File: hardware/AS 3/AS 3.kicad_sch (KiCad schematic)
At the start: 84 parts, among them J1 Conn_02x03_Odd_Even, J2 Conn_01x04, J3 USB_C_Receptacle_USB2.0_16P, Q1 PSMN5R2-60YL, SW1 SW_Push, SW2 SW_Push, U1 ESP32-S3-WROOM-1, U2 LM74610QDGKTQ1, U3 LMR604205SRAKRQ1, U4 TPS62901RPJR, U5 BME280, U6 TPS2121RUXR

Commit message: Update schematic
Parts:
- removed U5: BME280, BME280:PSON65P250X250X100-8N, symbol BME280:BME280
- added U5: BME280, Package_LGA:Bosch_LGA-8_2.5x2.5mm_P0.65mm_ClockwisePinNumbering, symbol Sensor:BME280
- C23: symbol PCM_JLCPCB-Capacitors:0603,100nF -> Device:C_Small
- C24: value 10uF -> 10u; symbol PCM_JLCPCB-Capacitors:1206,10uF -> Device:C_Small; Type X7R Ceramic -> (none)
- D1, D4, D5, D6, D7: value Green -> LED_Small
- R17, R6: value 4.7K -> 1k
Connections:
- net +3.3V: now also U5.2 (CSB), U5.6 (VDDIO), U5.8 (VDD)
- net GND: now also U3.7 (MODE_SYNC), U5.1 (GND), U5.5 (SDO), U5.7 (GND)
- net SCL: now also U5.4 (SCK)
- net SDA: now also U5.3 (SDI)
- net at R14.1, U3.8 (RT): no longer U3.7 (MODE_SYNC)
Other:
- moved on the sheet: C11, C12, C23, C24, R15, R16

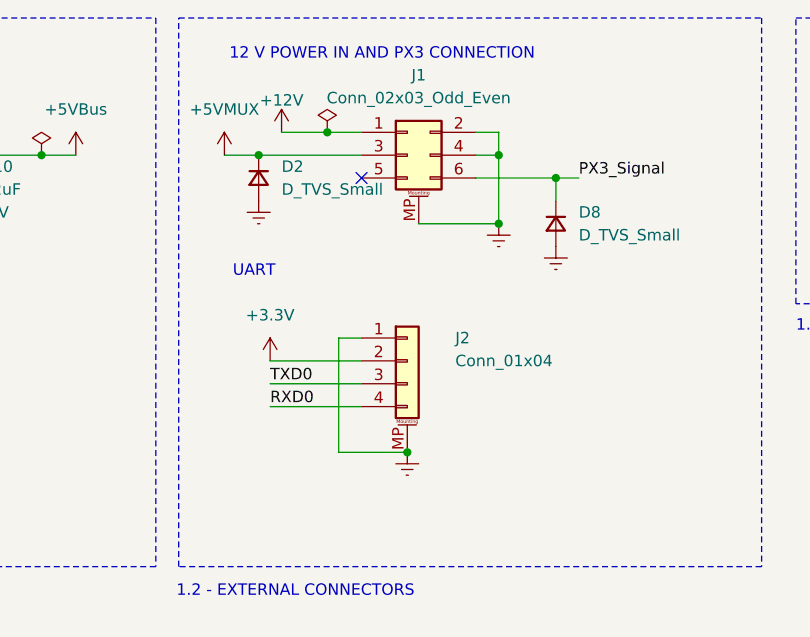
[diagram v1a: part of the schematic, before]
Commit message: time to make vias bigger and order this thing
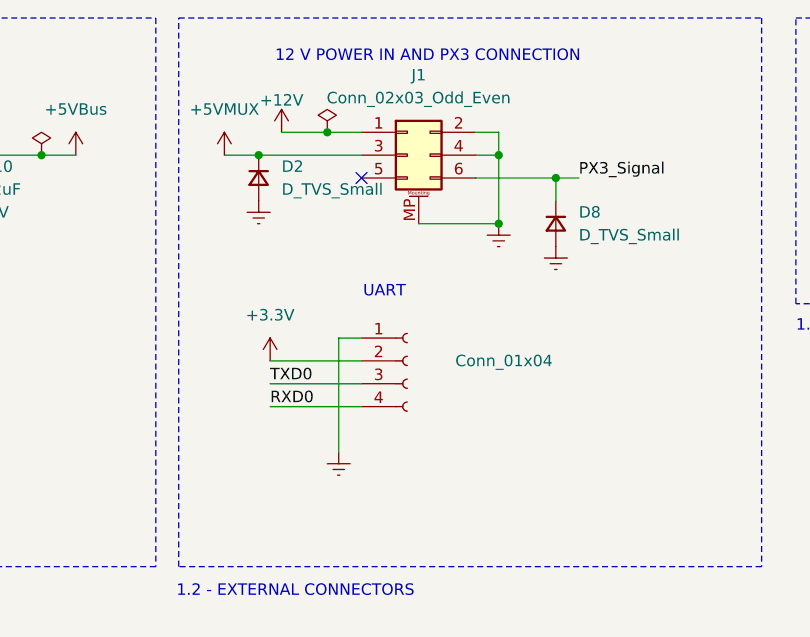
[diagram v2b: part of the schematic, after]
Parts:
- J2: footprint Connector_PinSocket_2.54mm:PinSocket_1x04_P2.54mm_Vertical_SMD_Pin1Left -> Connector_PinHeader_1.00mm:PinHeader_1x04_P1.00mm_Vertical; symbol Connector_Generic_MountingPin:Conn_01x04_MountingPin -> Connector:Conn_01x04_Socket
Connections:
- net GND: no longer J2.MP (MountPin)
